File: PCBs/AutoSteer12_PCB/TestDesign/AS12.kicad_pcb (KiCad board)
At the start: 2 copper layers, 159 x 152 mm, 79 parts, among them IC1 PCA9306DCUR, IC2 LM2576HVR-5.0, J1 ADS1115, J10 Conn_01x08_Female, J11 Teensy_Ethernet, J12 HR911105A, J13 Conn_01x15_Female, J14 Conn_01x08_Female, J15 Motor 2, J16 Motor 1, J17 SF_F9P_left, J18 ArduSimple_tl, J19 ArduSimple_bl, J2 WemosD1_left, J20 SF_F9P_right, J21 ArduSimple_tr, J22 ArduSimple_br, J23 Grove, J24 WemosD1_right, J3 DT13-12PA, J4 CMPS14, J5 BNO080_left, J6 BNO080_right, J7 I2C-3V3, J8 I2C-3V3, J9 Conn_01x15_Female, K1 HF3FF_012-1ZST, M1 CMPS14_no_pins, Q1 BC847, U1 PC817X2CSP9F, U2 PC817X2CSP9F, U3 PC817X2CSP9F, U4 CC6900SO-10A, U5 AZ1117H-3.3TRE1, U6 MAX3485EESA+T, U7 PC817X2CSP9F

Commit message: update pcb/software
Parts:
- removed U5: AZ1117H-3.3TRE1, Package_TO_SOT_SMD:SOT-223
- added C2: CL21B105KAFNNNE, Capacitor_SMD:C_0805_2012Metric, F.Cu at (82.8, 148.0)
- added D5: Zener Diode, Diode_SMD:D_SOD-123F, F.Cu at (149.9, 103.9)
- added D6: Zener Diode, Diode_SMD:D_SOD-123F, F.Cu at (149.9, 110.9)
- added IC3: AZ1117, Package_TO_SOT_SMD:SOT-223, F.Cu at (69.1, 112.1)
- added KF2: KF142V-5.0-2P, MyFootprints:KF142V-5.08-2P, F.Cu at (169.1, 98.6)
- added R13: 200, Resistor_SMD:R_1210_3225Metric, F.Cu at (149.9, 107.4)
- added R14: 200, Resistor_SMD:R_1210_3225Metric, F.Cu at (149.9, 100.4)
- C10: value VEJ102M1ETR-1313 -> RVT1V331M1010; footprint MyFootprints:CAPAE1300X1400N -> Capacitor_SMD:CP_Elec_10x10.5
- C9: value RVT1J101M1010 -> RVT1V471M1010; footprint Capacitor_SMD:CP_Elec_10x10 -> Capacitor_SMD:CP_Elec_10x10.5
- D4: footprint MyFootprints:1N4007 -> Diode_SMD:D_SMA
- IC2: value LM2576HVR-5.0 -> XL2596
- L1: value TMPA1265SP-101MN-D -> SMDRI127-330MT
- moved C10 19.2 mm to (86.1, 131.9), turned to 180 degrees
- moved R10 18.5 mm to (96.0, 105.9), turned to 0 degrees
- moved C7 18.2 mm to (62.1, 112.2)
- moved J8 13.8 mm to (140.2, 109.1), turned to 180 degrees
- moved L1 10.5 mm to (87.5, 118.6), turned to 0 degrees
- moved C6 10.1 mm to (65.9, 118.2)
- moved G*** 9.29 mm to (140.2, 105.6)
- moved D4 7.45 mm to (99.3, 136.2)
- moved IC1 6.94 mm to (133.0, 101.6)
- moved J7 5.67 mm to (140.2, 102.3), turned to 180 degrees
- moved C4 4.88 mm to (96.9, 120.0)
- moved R5 4.20 mm to (132.7, 106.1)
- moved REF** 2.93 mm to (129.4, 126.1)
- moved J4 2.93 mm to (101.8, 119.7)
- moved M1 2.93 mm to (98.8, 104.2)
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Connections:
- IC2 pad 6: (no net) -> GND
- U3 pad 4: Net-(J10-Pad2) -> Net-(J14-Pad3)
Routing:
- net Net-(J14-Pad3): track 0.00 -> 70.5 mm
- net Net-(J10-Pad2): track 61.1 -> 8.23 mm
- net Net-(D5-Pad1): track 0.00 -> 23.6 mm
- net Net-(D6-Pad1): track 0.00 -> 23.5 mm
- net Net-(Q1-Pad1): track 3.80 -> 23.8 mm
- net Net-(J9-Pad4): track 34.3 -> 16.2 mm
- net Net-(J10-Pad1): track 0.00 -> 16.0 mm
- net Net-(J10-Pad3): track 31.3 -> 43.6 mm
- net Net-(J10-Pad4): track 32.0 -> 44.0 mm
- net Net-(J10-Pad6): track 52.8 -> 64.5 mm
- net Net-(J10-Pad5): track 27.3 -> 38.7 mm
- net Net-(J10-Pad7): track 46.8 -> 58.1 mm
- net Net-(C2-Pad1): track 13.7 -> 23.9 mm
- net Net-(D2-Pad1): track 23.9 -> 32.8 mm
- net Net-(IC1-Pad5): track 77.0 -> 82.3 mm
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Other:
- board text added: "25"
- board text added: "26"
- board text added: "AS12 05-Jan-2022"

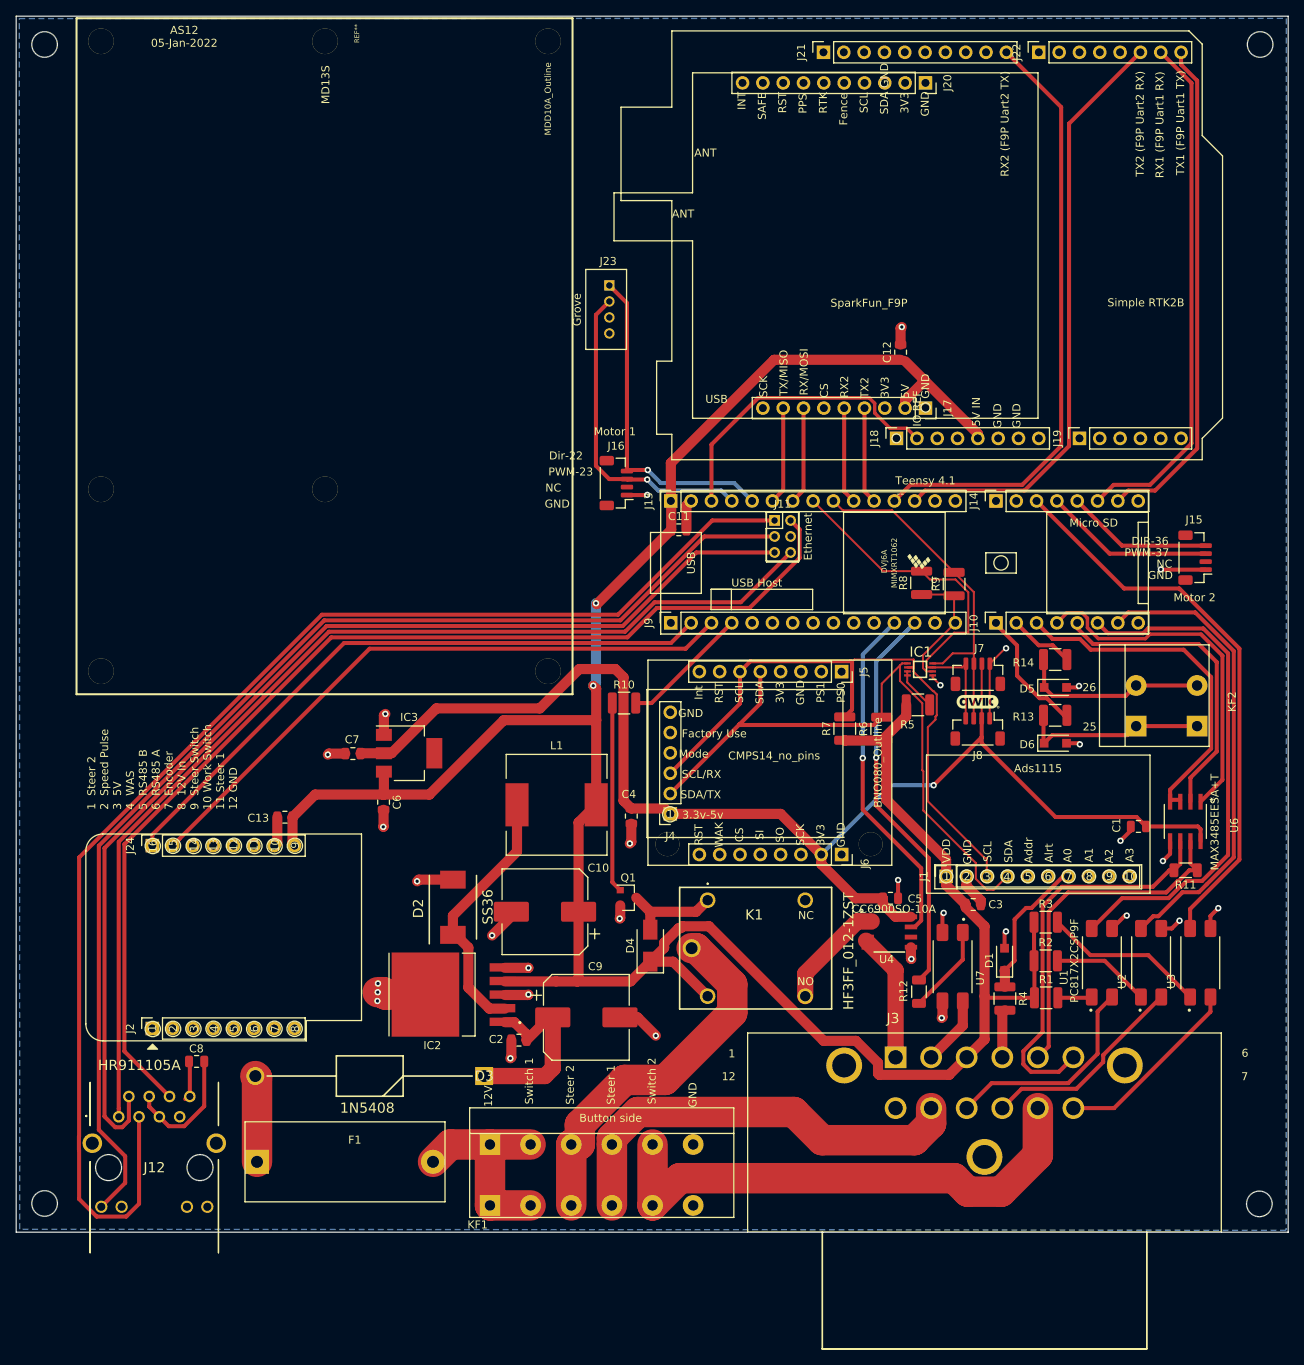
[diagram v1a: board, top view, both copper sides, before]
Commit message: fix board errors
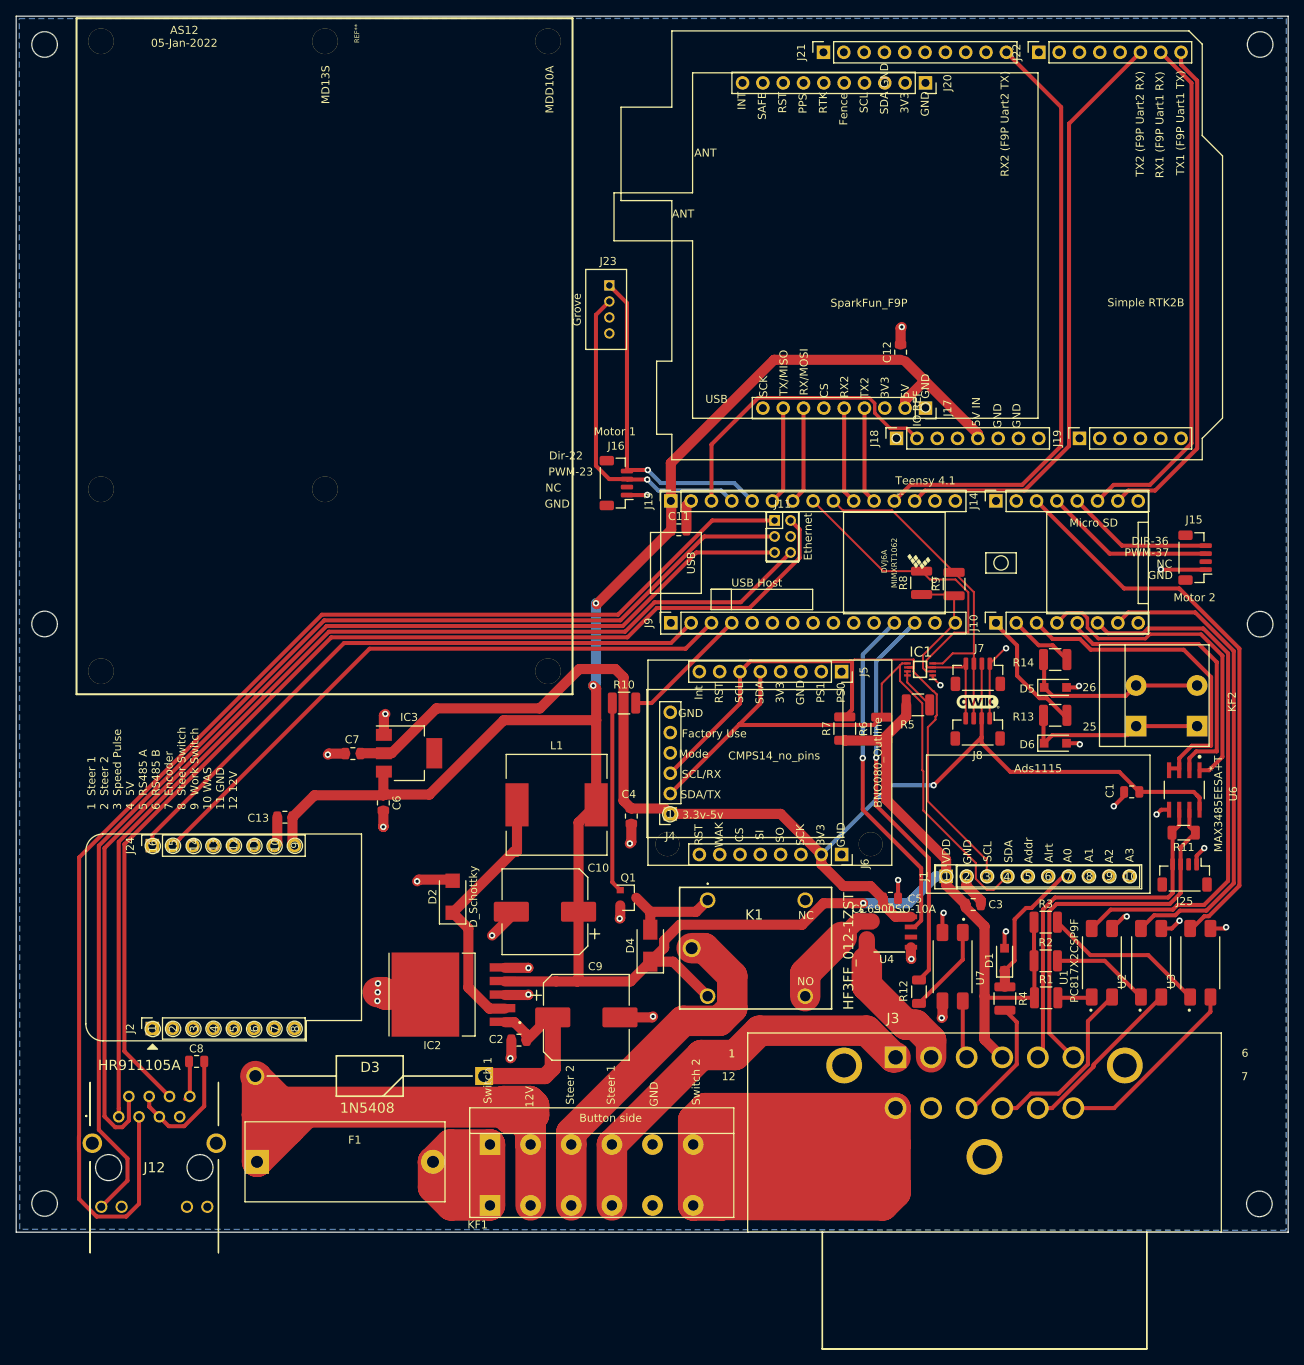
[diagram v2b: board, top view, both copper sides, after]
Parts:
- added  : , MountingHole:MountingHole_3.2mm_M3, F.Cu at (23.5, 96.0)
- added  : , MountingHole:MountingHole_3.2mm_M3, F.Cu at (175.5, 96.0)
- added J25: RS485, MyFootprints:Qwic_vertical, F.Cu at (166.1, 127.3)
- D2: value SS36 -> D_Schottky; footprint SamacSys_Parts:DIOM8059X265N -> MyFootprints:SMA(DO-214AC)
- REF**: value MDD10A_Outline -> MDD10A
- U6: footprint MyFootprints:MAX485ESA&plus_T -> MyFootprints:Maxim_Integrated-S8-2-0-P-MFG
- moved R11 4.71 mm to (165.9, 122.1)
- moved C1 4.40 mm to (159.4, 117.0)
- moved U6 3.94 mm to (166.0, 116.7)
- moved D2 1.32 mm to (74.6, 130.1)
- moved C6 0.09 mm to (65.9, 118.3)
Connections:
- J3 pad 11: Net-(J3-Pad11) -> GND
- J3 pad 12: GND -> Net-(J3-Pad12)
- J3 pad 3: Net-(C10-Pad1) -> Net-(J3-Pad3)
- J3 pad 4: Net-(J3-Pad4) -> Net-(C10-Pad1)
- J3 pad 5: Net-(J3-Pad5) -> Net-(J25-Pad4)
- J3 pad 6: Net-(J3-Pad6) -> Net-(J25-Pad3)
- KF1 pad 2: Net-(F1-Pad2) -> Net-(D3-Pad2)
- KF1 pad 4: Net-(J3-Pad11) -> Net-(J3-Pad1)
- KF1 pad 5: Net-(J3-Pad8) -> GND
- KF1 pad 6: GND -> Net-(J3-Pad12)
- R11 pad 1: Net-(J3-Pad5) -> Net-(J25-Pad3)
- R11 pad 2: Net-(J3-Pad6) -> Net-(J25-Pad4)
- R4 pad 2: Net-(J3-Pad4) -> Net-(J3-Pad10)
- U1 pad 2: Net-(J3-Pad10) -> Net-(J3-Pad9)
- U2 pad 2: Net-(J3-Pad9) -> Net-(J3-Pad8)
- U4 pad 3: Net-(J3-Pad1) -> Net-(J3-Pad2)
- U4 pad 4: Net-(J3-Pad1) -> Net-(J3-Pad2)
- U6 pad 6: Net-(J3-Pad6) -> Net-(J25-Pad4)
- U6 pad 7: Net-(J3-Pad5) -> Net-(J25-Pad3)
- U7 pad 4: Net-(J3-Pad2) -> Net-(J3-Pad3)
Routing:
- net Net-(J3-Pad12): track 0.00 -> 171.4 mm
- net Net-(D3-Pad2): track 10.8 -> 114.5 mm
- net Net-(J3-Pad11): track 53.9 -> 0.00 mm
- net Net-(J3-Pad6): track 50.4 -> 0.00 mm
- net Net-(J25-Pad3): track 0.00 -> 48.4 mm
- net Net-(J25-Pad4): track 0.00 -> 46.6 mm
- net Net-(J3-Pad8): track 65.7 -> 21.3 mm
- net Net-(J3-Pad5): track 43.5 -> 0.00 mm
- net Net-(J3-Pad1): track 16.1 -> 50.3 mm
- net Net-(F1-Pad2): track 25.8 -> 41.5 mm
- net Net-(J3-Pad10): track 27.0 -> 15.9 mm
- net Net-(J3-Pad2): track 8.68 -> 18.8 mm
- net Net-(C10-Pad1): track 323.4 -> 314.9 mm, vias 2 -> 3
- net Net-(J3-Pad3): track 0.00 -> 7.24 mm
- net Net-(K1-Pad4): track 13.8 -> 20.3 mm
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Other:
- board text added: "1 Steer 1 2 Steer 2 3 Speed Pulse 4 5V 5 RS485 A 6 RS485 B 7 Encoder 8 Steer Switch 9 Work Switch 10 WAS 11 GND 12 12V"
- board text removed: "1 Steer 2 2 Speed Pulse 3 5V 4 WAS 5 RS485 B 6 RS485 A 7 Encoder 8 12V In 9 Steer Switch 10 Work Switch 11 Steer 1 12 GND"
